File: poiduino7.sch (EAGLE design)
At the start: 17 parts, among them Y1 16MHZ

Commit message: add gitignore and new board
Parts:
- added C6, C7: 0.1uf, Seeed-Capacitor:DIP-CERAMIC-DISC-10NF-50V-Y5V(D4.0MM)
- added K1: TS-1109, Seeed-OPL-Button:DIP-BUTTON-4P
- C1, C2: value 10nf -> 18pf
- C3, C4: value 10nf -> 0.1uf
- C5: value 100uf -> 1uf
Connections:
- removed net N$10: U1.GND
- removed net N$11: U1.VCC@1
- removed net N$12: U1.GND@1
- removed net N$13: U1.(SCK)PB5
- removed net N$14: U1.(MISO)PB4
- removed net N$15: U1.(MOSI/OC2)PB3
- removed net N$16: U1.(SS/OC1B)PB2
- removed net N$17: U1.(OC1A)PB1
- removed net N$18: U1.(ICP)PB0
- removed net N$19: U1.(ADC4/SDA)PC4
- removed net N$2: C2.2, Y1.1
- removed net N$20: U1.(ADC3)PC3
- removed net N$21: U1.(ADC2)PC2
- removed net N$22: U1.(ADC1)PC1
- removed net N$23: U1.(ADC0)PC0
- removed net N$24: U1.(AIN1)PD7
- removed net N$25: U1.(AIN0)PD6
- removed net N$26: U1.(T1)PD5
- removed net N$27: U1.(XCK/T0)PD4
- removed net N$28: U1.(INT1)PD3
- removed net N$29: U1.(INT0)PD2
- removed net N$30: U1.(TXD)PD1
- removed net N$31: U1.(RXD)PD0
- removed net N$4: U1.(ADC5/SCL)PC5
- removed net N$5: U1.PB6(XTAL1/TOSC1)
- removed net N$7: U1.PC6(/!RESET)
- removed net N$8: U1.AREF
- removed net N$9: U1.AVCC
- new net A0: JP5.1, U1.(ADC0)PC0
- new net A1: JP5.2, U1.(ADC1)PC1
- new net A2: JP5.3, U1.(ADC2)PC2
- new net A3: JP5.4, U1.(ADC3)PC3
- new net A4-SDA: JP5.5, U1.(ADC4/SDA)PC4
- new net A5-SCL: JP5.6, U1.(ADC5/SCL)PC5
- new net AREF: C4.2, JP3.1, U1.AREF
- new net AVCC: C7.2, U1.AVCC
- new net CTS: JP1.5
- new net DTR: C6.2, JP1.1
- new net N$34: JP2.1
- new net N$38: JP2.5
- new net PIN10: JP3.6, U1.(SS/OC1B)PB2
- new net PIN11: JP3.5, U1.(MOSI/OC2)PB3
- new net PIN12: JP3.4, U1.(MISO)PB4
- new net PIN13: JP3.3, R2.2, U1.(SCK)PB5
- new net PIN2: JP4.3, U1.(INT0)PD2
- new net PIN3: JP4.4, U1.(INT1)PD3
- new net PIN4: JP4.5, U1.(XCK/T0)PD4
- new net PIN5: JP4.6, U1.(T1)PD5
- new net PIN6: JP4.7, U1.(AIN0)PD6
- new net PIN7: JP4.8, U1.(AIN1)PD7
- new net PIN8: JP3.8, U1.(ICP)PB0
- new net PIN9: JP3.7, U1.(OC1A)PB1
- new net RESET: C6.1, JP2.6, K1.A0, K1.A1, R1.2, U1.PC6(/!RESET)
- new net RXD: JP1.2, JP4.1, U1.(RXD)PD0
- new net TXD: JP1.3, JP4.2, U1.(TXD)PD1
- new net VCC: C3.2, C5.+, C7.1, JP1.4, JP2.4, R1.1, R3.1, U1.VCC@1
- new net XTAL1: C2.2, U1.PB6(XTAL1/TOSC1), Y1.1
- new net XTAL2: C1.2, U1.PB7(XTAL2/TOSC2), Y1.2
- net GND: now also C3.1, C4.1, C5.-, D1.-, D2.-, JP1.6, JP2.2, JP2.3, JP3.2, K1.B0, U1.GND, U1.GND@1
- net N$3: now also D2.+, R3.2; no longer C1.2, Y1.2
- net N$6: now also D1.+, R2.1; no longer U1.PB7(XTAL2/TOSC2)
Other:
- moved on the sheet: C1, C2, C3, C4, C5, D1, D2, JP1, JP2, JP3, JP4, JP5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

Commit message: new board
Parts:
- C7: device Seeed-Capacitor:DIP-CERAMIC-DISC-10NF-50V-Y5V(D4.0MM) -> capacitor-wima:C5/2.5
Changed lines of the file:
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@@
 <?xml version="1.0" encoding="utf-8"?>
 <!DOCTYPE eagle SYSTEM "eagle.dtd">
-<eagle version="7.7.0">
+<eagle version="9.0.0">
 <drawing>
 <settings>
 <setting alwaysvectorfont="no"/>
+<setting keepoldvectorfont="yes"/>
 <setting verticaltext="up"/>
 </settings>
-<grid distance="0.05" unitdist="inch" unit="inch" style="lines" multiple="1" display="yes" altdistance="0.001" altunitdist="inch" altunit="inch"/>
+<grid distance="0.1" unitdist="inch" unit="inch" style="lines" multiple="1" display="no" altdistance="0.01" altunitdist="inch" altunit="inch"/>
 <layers>
 <layer number="1" name="Top" color="4" fill="1" visible="no" active="no"/>
@@
 <part name="D1" library="Seeed-LED" deviceset="DIP-LED-GREEN-GREEN(2P-D3MM)" device="" value="CX-G302DC"/>
 <part name="D2" library="Seeed-LED" deviceset="DIP-LED-GREEN-GREEN(2P-D3MM)" device="" value="CX-G302DC"/>
-<part name="U1" library="Seeed-IC" deviceset="MCU-ATMEGA328P-PU(DIP28)" device=""/>
+<part name="U1" library="Seeed-IC" library_urn="urn:adsk.eagle:library:470" deviceset="MCU-ATMEGA328P-PU(DIP28)" device="" package3d_urn="urn:adsk.eagle:package:32652/1"/>
 <part name="Y1" library="Seeed-Crystal Oscillator" deviceset="DIP-CRYSTAL-16MHZ-18PF-30PPM-40R(HC49US)" device="" value="16MHZ"/>
 <part name="R1" library="Seeed-Resistor" deviceset="DIP-RES-10K-5%-1/4W(PR-D2.3XL6.5MM)" device="" value="10K"/>
@@
 <part name="SUPPLY7" library="supply2" deviceset="GND" device=""/>
 <part name="P+3" library="supply1" deviceset="VCC" device=""/>
-<part name="C7" library="Seeed-Capacitor" deviceset="DIP-CERAMIC-DISC-10NF-50V-Y5V(D4.0MM)" device="" value="0.1uf"/>
+<part name="C7" library="capacitor-wima" library_urn="urn:adsk.eagle:library:116" deviceset="C" device="5/2.5" package3d_urn="urn:adsk.eagle:package:5426/1" value="0.1uf"/>
 </parts>
 <sheets>
@@
 <instance part="SUPPLY7" gate="GND" x="77.47" y="81.28"/>
 <instance part="P+3" gate="VCC" x="77.47" y="109.22"/>
-<instance part="C7" gate="G$1" x="67.31" y="-16.51" rot="R90"/>
+<instance part="C7" gate="G$1" x="67.31" y="-16.51" rot="R180"/>
 </instances>
 <busses>
@@
 <label x="85.09" y="-10.16" size="1.27" layer="95" rot="R180" xref="yes"/>
 <pinref part="C7" gate="G$1" pin="2"/>
-<wire x1="67.31" y1="-12.7" x2="67.31" y2="-10.16" width="0.1524" layer="91"/>
+<wire x1="67.31" y1="-11.43" x2="67.31" y2="-10.16" width="0.1524" layer="91"/>
 <wire x1="91.44" y1="-10.16" x2="67.31" y2="-10.16" width="0.1524" layer="91"/>
 </segment>
@@
 <label x="85.09" y="-22.86" size="1.27" layer="95" rot="R180" xref="yes"/>
 <pinref part="C7" gate="G$1" pin="1"/>
-<wire x1="67.31" y1="-20.32" x2="67.31" y2="-22.86" width="0.1524" layer="91"/>
+<wire x1="67.31" y1="-19.05" x2="67.31" y2="-22.86" width="0.1524" layer="91"/>
 <wire x1="67.31" y1="-22.86" x2="91.44" y2="-22.86" width="0.1524" layer="91"/>
 </segment>
@@
 </schematic>
 </drawing>
+<compatibility>
+<note version="8.2" severity="warning">
+Since Version 8.2, EAGLE supports online libraries. The ids
+of those online libraries will not be understood (or retained)
+with this version.
+</note>
+<note version="8.3" severity="warning">
+Since Version 8.3, EAGLE supports URNs for individual library
+assets (packages, symbols, and devices). The URNs of those assets
+will not be understood (or retained) with this version.
+</note>
+<note version="8.3" severity="warning">
+Since Version 8.3, EAGLE supports the association of 3D packages
+with devices in libraries, schematics, and board files. Those 3D
+packages will not be understood (or retained) with this version.
+</note>
+</compatibility>
 </eagle>

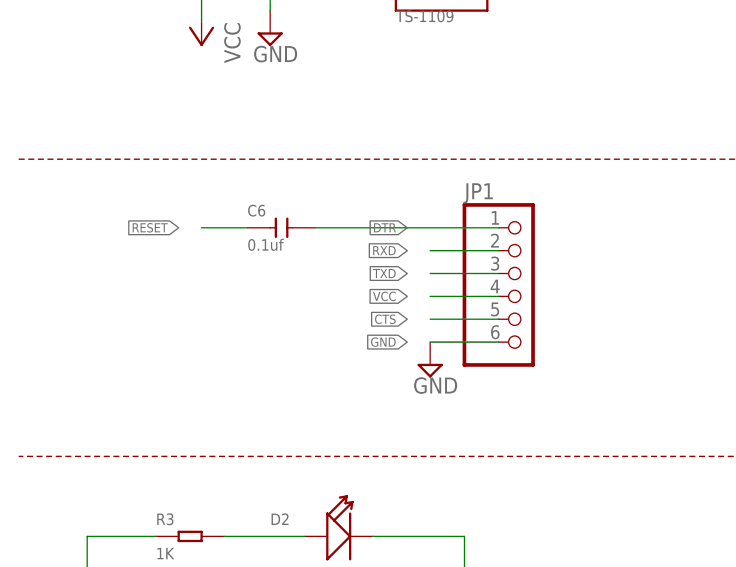
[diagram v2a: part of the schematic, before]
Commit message: rename file and folders, generate gcode and simulate files for Roland
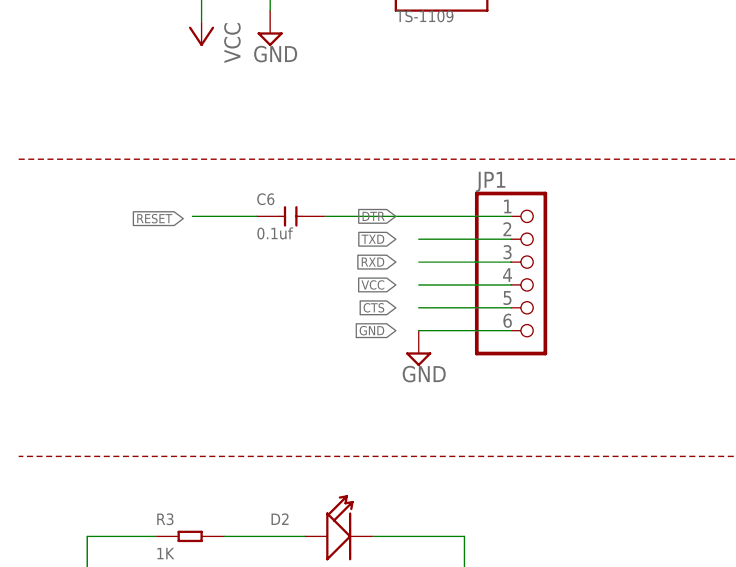
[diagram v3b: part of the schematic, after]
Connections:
- net RXD: now also JP1.3; no longer JP1.2
- net TXD: now also JP1.2; no longer JP1.3
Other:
- moved on the sheet: C6, JP1
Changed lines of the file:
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@@
 <setting verticaltext="up"/>
 </settings>
-<grid distance="0.1" unitdist="inch" unit="inch" style="lines" multiple="1" display="no" altdistance="0.01" altunitdist="inch" altunit="inch"/>
+<grid distance="0.1" unitdist="inch" unit="inch" style="lines" multiple="1" display="yes" altdistance="0.01" altunitdist="inch" altunit="inch"/>
 <layers>
 <layer number="1" name="Top" color="4" fill="1" visible="no" active="no"/>
@@
 </plain>
 <instances>
-<instance part="JP1" gate="A" x="-44.45" y="46.99"/>
+<instance part="JP1" gate="A" x="-43.08" y="48.26"/>
 <instance part="JP2" gate="A" x="20.32" y="25.4"/>
 <instance part="JP3" gate="A" x="20.32" y="-2.54"/>
@@
 <instance part="SUPPLY2" gate="GND" x="-72.39" y="76.2"/>
 <instance part="P+1" gate="VCC" x="-80.01" y="74.93" rot="R180"/>
-<instance part="SUPPLY3" gate="GND" x="-54.61" y="39.37"/>
-<instance part="C6" gate="G$1" x="-71.12" y="54.61"/>
+<instance part="SUPPLY3" gate="GND" x="-55.88" y="40.64"/>
+<instance part="C6" gate="G$1" x="-70.104" y="55.88"/>
 <instance part="SUPPLY4" gate="GND" x="-50.8" y="11.43"/>
 <instance part="P+2" gate="VCC" x="-92.71" y="10.16" rot="R180"/>
@@
 <segment>
 <pinref part="JP1" gate="A" pin="6"/>
-<wire x1="-46.99" y1="41.91" x2="-54.61" y2="41.91" width="0.1524" layer="91"/>
-<label x="-57.15" y="41.91" size="1.016" layer="95" rot="R180" xref="yes"/>
+<wire x1="-45.62" y1="43.18" x2="-55.88" y2="43.18" width="0.1524" layer="91"/>
+<label x="-58.42" y="43.18" size="1.016" layer="95" rot="R180" xref="yes"/>
 <pinref part="SUPPLY3" gate="GND" pin="GND"/>
 </segment>
@@
 <segment>
 <pinref part="C6" gate="G$1" pin="1"/>
-<wire x1="-74.93" y1="54.61" x2="-80.01" y2="54.61" width="0.1524" layer="91"/>
-<label x="-82.55" y="54.61" size="1.016" layer="95" rot="R180" xref="yes"/>
+<wire x1="-73.914" y1="55.88" x2="-81.026" y2="55.88" width="0.1524" layer="91"/>
+<label x="-82.042" y="55.626" size="1.016" layer="95" rot="R180" xref="yes"/>
 </segment>
 <segment>
@@
 <segment>
 <pinref part="JP1" gate="A" pin="4"/>
-<wire x1="-46.99" y1="46.99" x2="-54.61" y2="46.99" width="0.1524" layer="91"/>
-<label x="-57.15" y="46.99" size="1.016" layer="95" rot="R180" xref="yes"/>
+<wire x1="-45.62" y1="48.26" x2="-55.88" y2="48.26" width="0.1524" layer="91"/>
+<label x="-58.42" y="48.26" size="1.016" layer="95" rot="R180" xref="yes"/>
 </segment>
 <segment>
@@
 <net name="RXD" class="0">
 <segment>
-<pinref part="JP1" gate="A" pin="2"/>
-<wire x1="-46.99" y1="52.07" x2="-54.61" y2="52.07" width="0.1524" layer="91"/>
-<label x="-57.15" y="52.07" size="1.016" layer="95" rot="R180" xref="yes"/>
-</segment>
-<segment>
 <pinref part="U1" gate="G$1" pin="(RXD)PD0"/>
 <wire x1="142.24" y1="-45.72" x2="148.59" y2="-45.72" width="0.1524" layer="91"/>
@@
 <wire x1="17.78" y1="-22.86" x2="7.62" y2="-22.86" width="0.1524" layer="91"/>
 </segment>
+<segment>
+<label x="-58.42" y="50.8" size="1.016" layer="95" rot="R180" xref="yes"/>
+<pinref part="JP1" gate="A" pin="3"/>
+<wire x1="-45.62" y1="50.8" x2="-55.88" y2="50.8" width="0.1524" layer="91"/>
+</segment>
 </net>
 <net name="TXD" class="0">
-<segment>
-<pinref part="JP1" gate="A" pin="3"/>
-<wire x1="-46.99" y1="49.53" x2="-54.61" y2="49.53" width="0.1524" layer="91"/>
-<label x="-57.15" y="49.53" size="1.016" layer="95" rot="R180" xref="yes"/>
-</segment>
 <segment>
 <pinref part="U1" gate="G$1" pin="(TXD)PD1"/>
@@
 <pinref part="JP4" gate="A" pin="2"/>
 </segment>
+<segment>
+<label x="-58.42" y="53.34" size="1.016" layer="95" rot="R180" xref="yes"/>
+<pinref part="JP1" gate="A" pin="2"/>
+<wire x1="-45.62" y1="53.34" x2="-55.88" y2="53.34" width="0.1524" layer="91"/>
+</segment>
 </net>
 <net name="CTS" class="0">
 <segment>
 <pinref part="JP1" gate="A" pin="5"/>
-<wire x1="-46.99" y1="44.45" x2="-54.61" y2="44.45" width="0.1524" layer="91"/>
-<label x="-57.15" y="44.45" size="1.016" layer="95" rot="R180" xref="yes"/>
+<wire x1="-45.62" y1="45.72" x2="-55.88" y2="45.72" width="0.1524" layer="91"/>
+<label x="-58.42" y="45.72" size="1.016" layer="95" rot="R180" xref="yes"/>
 </segment>
 </net>
@@
 <segment>
 <pinref part="JP1" gate="A" pin="1"/>
-<label x="-57.15" y="54.61" size="1.016" layer="95" rot="R180" xref="yes"/>
+<label x="-58.42" y="55.88" size="1.016" layer="95" rot="R180" xref="yes"/>
 <pinref part="C6" gate="G$1" pin="2"/>
-<wire x1="-67.31" y1="54.61" x2="-46.99" y2="54.61" width="0.1524" layer="91"/>
-</segment>
-</net>
+<wire x1="-66.294" y1="55.88" x2="-45.62" y2="55.88" width="0.1524" layer="91"/>
+</segment>
+</net>
